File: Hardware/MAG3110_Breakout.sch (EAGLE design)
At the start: 17 parts, among them U1 MAG31101:1

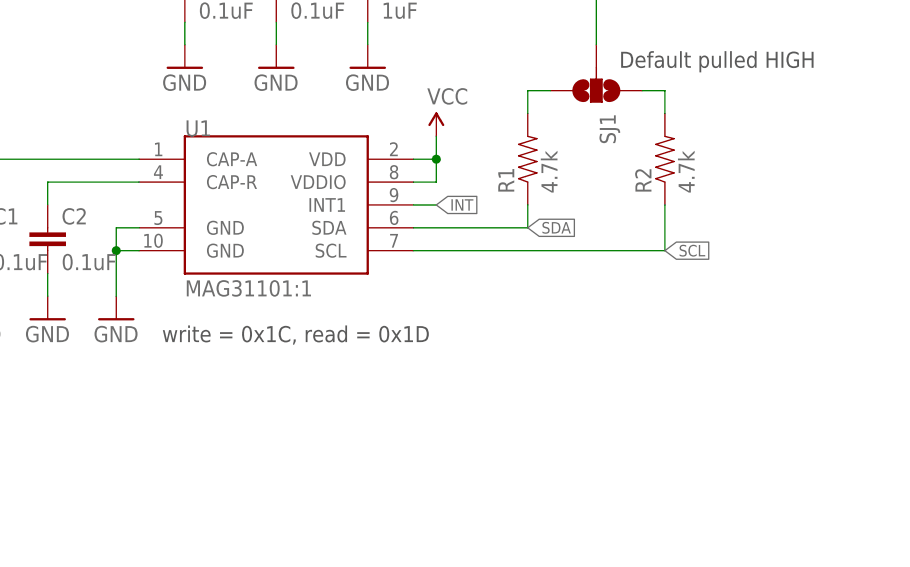
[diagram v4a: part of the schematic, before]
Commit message: Silk updates
1.) Added axis silk to bottom.
2.) Added SFE flame to top silk.
3.) Moved existing silk to accommodate additions.
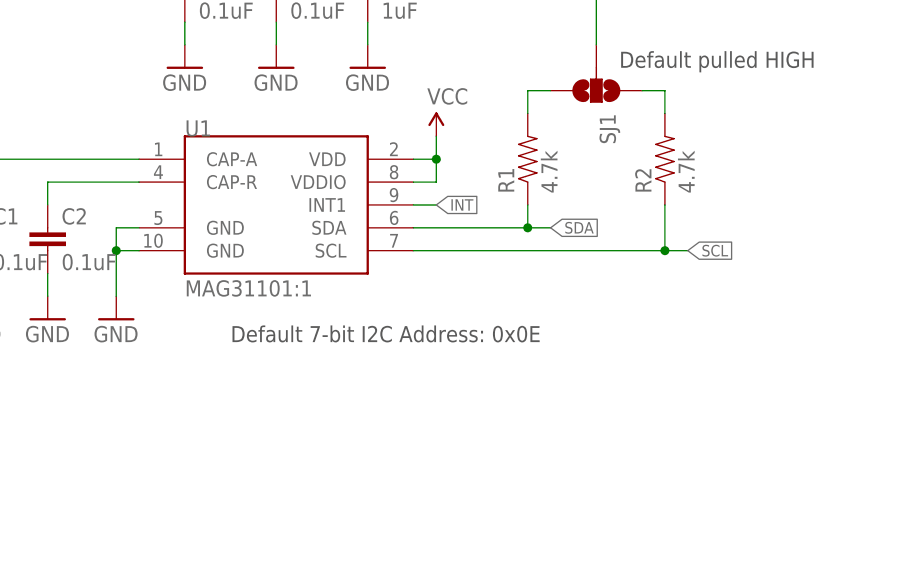
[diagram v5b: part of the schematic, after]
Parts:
- renumbered JP4 to JP7
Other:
- note added: "Default 7-bit I2C Address: 0x0E"
- note removed: "write = 0x1C, read = 0x1D"
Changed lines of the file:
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@@
 <part name="JP2" library="SparkFun" deviceset="STAND-OFF" device=""/>
 <part name="JP3" library="SparkFun" deviceset="STAND-OFF" device=""/>
-<part name="JP4" library="SparkFun" deviceset="LOGO-SFE" device="SK"/>
+<part name="JP7" library="SparkFun" deviceset="LOGO-SFE" device="SK"/>
 <part name="JP5" library="abes" deviceset="FIDUCIAL" device="1X2.5"/>
 <part name="JP6" library="abes" deviceset="FIDUCIAL" device="1X2.5"/>
@@
 <sheet>
 <plain>
-<text x="111.76" y="71.12" size="1.778" layer="97">write = 0x1C, read = 0x1D</text>
 <text x="241.3" y="7.62" size="2.54" layer="94" ratio="15">12</text>
 <text x="167.64" y="10.16" size="2.54" layer="94" ratio="15">Kade Jensen</text>
 <text x="162.56" y="101.6" size="1.778" layer="97">Default pulled HIGH</text>
+<text x="119.38" y="71.12" size="1.778" layer="97">Default 7-bit I2C Address: 0x0E</text>
 </plain>
 <instances>
@@
 <instance part="JP2" gate="G$1" x="246.38" y="25.4"/>
 <instance part="JP3" gate="G$1" x="246.38" y="33.02"/>
-<instance part="JP4" gate="G$1" x="236.22" y="27.94"/>
+<instance part="JP7" gate="G$1" x="236.22" y="27.94"/>
 <instance part="JP5" gate="G$1" x="228.6" y="25.4"/>
 <instance part="JP6" gate="G$1" x="228.6" y="33.02"/>
@@
 <pinref part="U1" gate="G$1" pin="SDA"/>
 <wire x1="152.4" y1="83.82" x2="139.7" y2="83.82" width="0.1524" layer="91"/>
-<label x="152.4" y="83.82" size="1.27" layer="95" xref="yes"/>
+<wire x1="152.4" y1="83.82" x2="154.94" y2="83.82" width="0.1524" layer="91"/>
+<junction x="152.4" y="83.82"/>
+<label x="154.94" y="83.82" size="1.27" layer="95" xref="yes"/>
 </segment>
 <segment>
@@
 <pinref part="U1" gate="G$1" pin="SCL"/>
 <wire x1="139.7" y1="81.28" x2="167.64" y2="81.28" width="0.1524" layer="91"/>
-<label x="167.64" y="81.28" size="1.27" layer="95" xref="yes"/>
+<wire x1="167.64" y1="81.28" x2="170.18" y2="81.28" width="0.1524" layer="91"/>
+<junction x="167.64" y="81.28"/>
+<label x="170.18" y="81.28" size="1.27" layer="95" xref="yes"/>
 </segment>
 <segment>

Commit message: changed fiducials
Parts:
- removed JP5, JP6: FIDUCIAL1X2.5, abes:FIDUCIAL1X2.5
- added FID1, FID2: FIDUCIAL1X2, SparkFun-Aesthetics:FIDUCIAL1X2
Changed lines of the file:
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@@
 <part name="JP3" library="SparkFun" deviceset="STAND-OFF" device=""/>
 <part name="JP7" library="SparkFun" deviceset="LOGO-SFE" device="SK"/>
-<part name="JP5" library="abes" deviceset="FIDUCIAL" device="1X2.5"/>
-<part name="JP6" library="abes" deviceset="FIDUCIAL" device="1X2.5"/>
 <part name="FRAME2" library="SparkFun-Aesthetics" deviceset="FRAME-LETTER" device=""/>
 <part name="LOGO1" library="SparkFun-Aesthetics" deviceset="OSHW-LOGO" device="S"/>
@@
 <part name="GND8" library="SparkFun" deviceset="GND" device=""/>
 <part name="SJ1" library="SparkFun-Passives" deviceset="SOLDERJUMPER_2WAY" device="PASTE1&amp;2&amp;3"/>
+<part name="FID1" library="SparkFun-Aesthetics" deviceset="FIDUCIAL" device="1X2"/>
+<part name="FID2" library="SparkFun-Aesthetics" deviceset="FIDUCIAL" device="1X2"/>
 </parts>
 <sheets>
@@
 <instance part="JP3" gate="G$1" x="246.38" y="33.02"/>
 <instance part="JP7" gate="G$1" x="236.22" y="27.94"/>
-<instance part="JP5" gate="G$1" x="228.6" y="25.4"/>
-<instance part="JP6" gate="G$1" x="228.6" y="33.02"/>
 <instance part="FRAME2" gate="G$1" x="0" y="0"/>
 <instance part="FRAME2" gate="G$2" x="147.32" y="0"/>
@@
 <instance part="GND8" gate="1" x="134.62" y="101.6"/>
 <instance part="SJ1" gate="G$1" x="160.02" y="99.06" rot="R270"/>
+<instance part="FID1" gate="G$1" x="223.52" y="33.02"/>
+<instance part="FID2" gate="G$1" x="223.52" y="25.4"/>
 </instances>
 <busses>
